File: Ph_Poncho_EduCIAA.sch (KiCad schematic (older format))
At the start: 26 parts, among them P1 BNC, U1 TC1121COA, U2 CA3140, U3 TL081

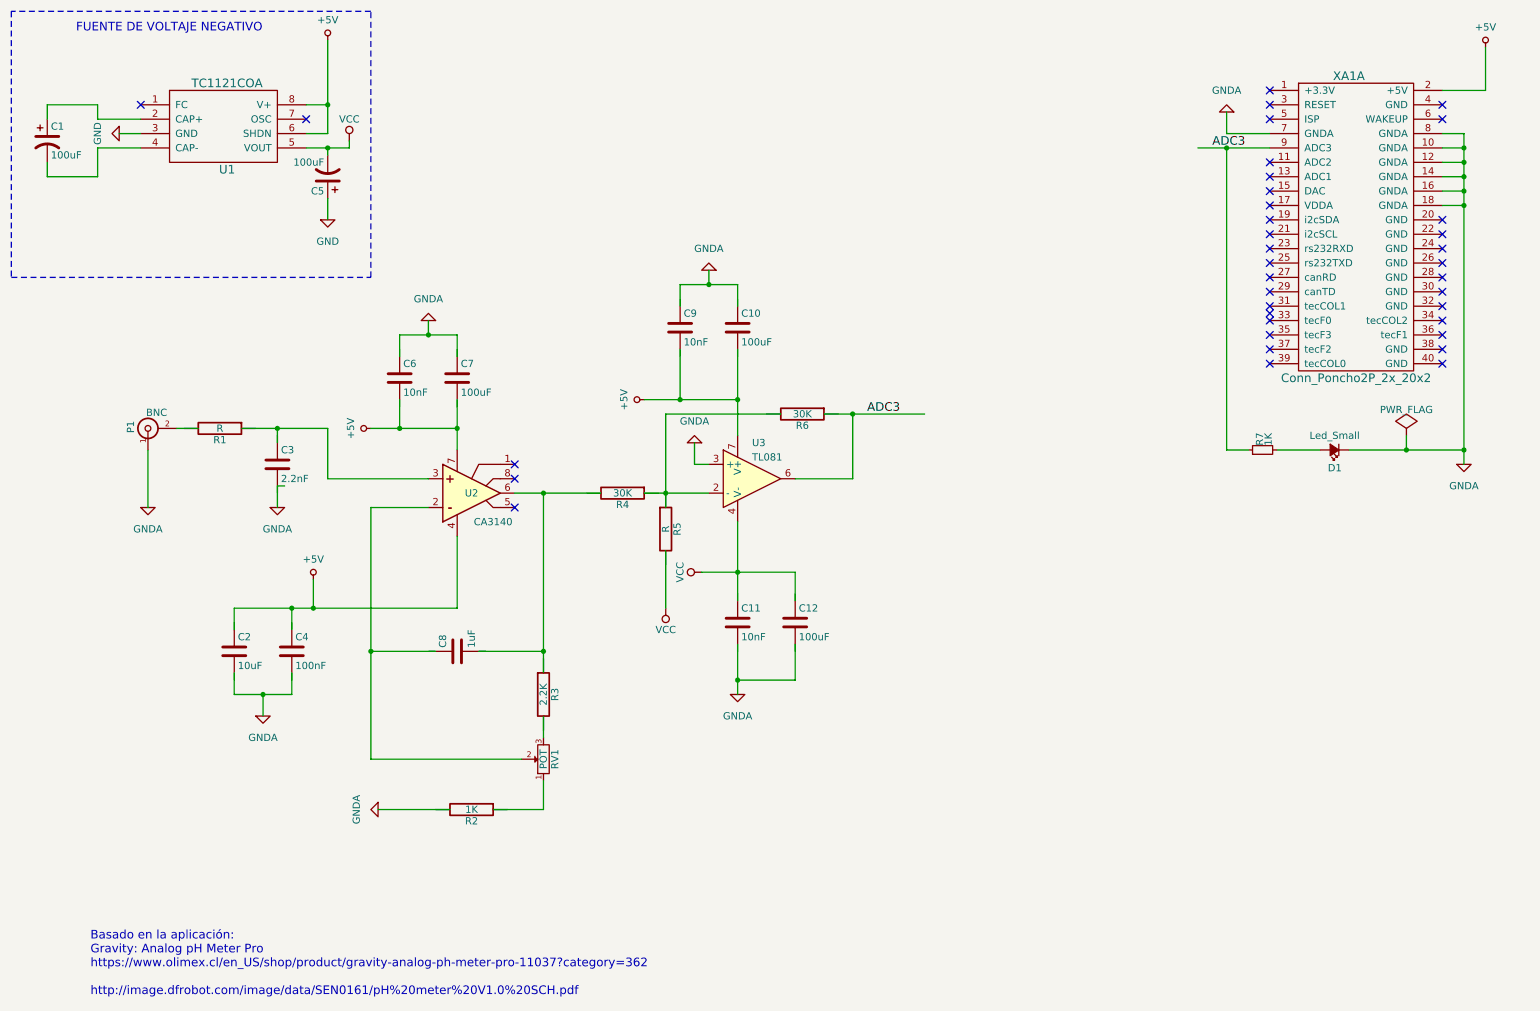
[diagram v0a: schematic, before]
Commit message: Se cambió el inversor de voltaje TC1121COA por el LMC7660
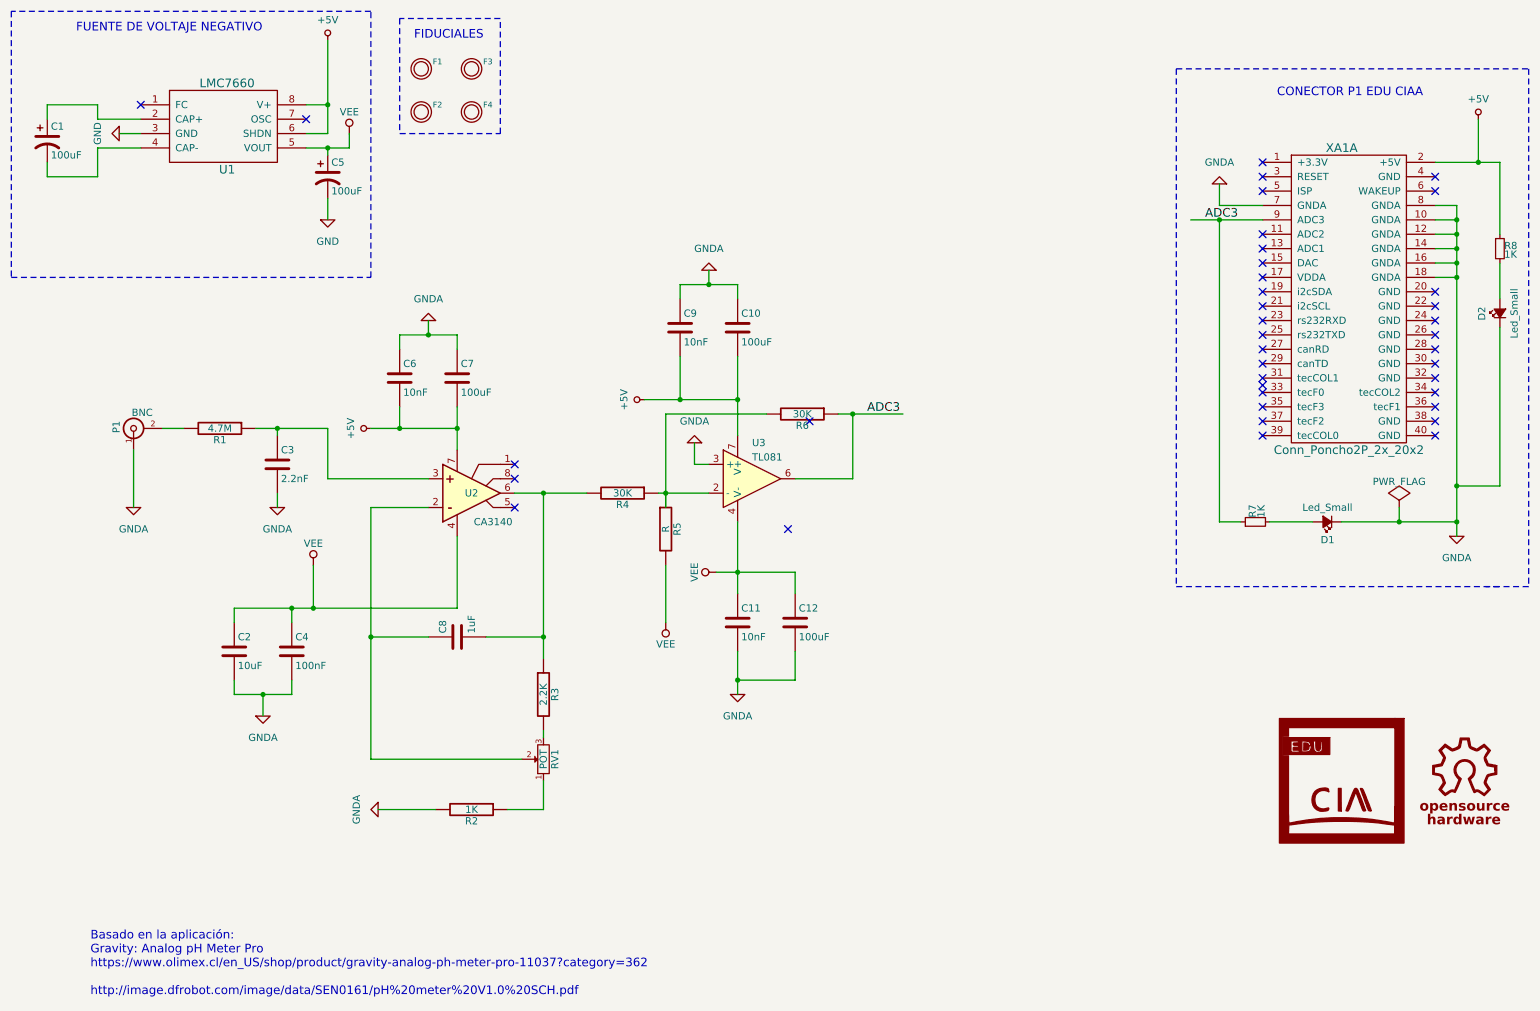
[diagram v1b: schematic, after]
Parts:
- removed U1: TC1121COA, symbol TC1121COA
- added D2: Led_Small, Ph_Poncho:LED_1206, symbol Led_Small
- added F1, F2, F3, F4: FIDUCIAL, Ph_Poncho:Fiducial_1mm, symbol FIDUCIAL
- added R8: 1K, Ph_Poncho:R_1206_HandSoldering, symbol R_Small
- added U1: LMC7660, symbol LMC7660
- C1: footprint (none) -> Ph_Poncho:CP_Elec_6.3x4.5; Digikey# Value -> 493-2203-1-ND; LibPart Value -> (none); Manf Value -> Nichicon; Manf# Value -> UWT1V101MCL1GS
- C10, C11, C12, C2, C3, C4, C6, C7, C8, C9: footprint (none) -> Ph_Poncho:C_1206_HandSoldering
- C5: footprint (none) -> Ph_Poncho:CP_Elec_6.3x4.5
- D1: footprint (none) -> Ph_Poncho:LED_1206; Digikey# (none) -> Value; LibPart (none) -> Value; Manf (none) -> Value; Manf# (none) -> Value; Mouser# (none) -> Value
- P1: footprint (none) -> Ph_Poncho:BNC_Socket_TYCO-AMP; Digikey# (none) -> A32244-ND; LibPart (none) -> Value; Manf (none) -> TE Connectivity AMP Connectors; Manf# (none) -> 5227161-1; Mouser# (none) -> Value
- R1: value R -> 4.7M; footprint (none) -> Ph_Poncho:R_1206_HandSoldering; Digikey# (none) -> Value; LibPart (none) -> Value; Manf (none) -> Value; Manf# (none) -> Value; Mouser# (none) -> Value
- R2, R3, R4, R5, R6, R7: footprint (none) -> Ph_Poncho:R_1206_HandSoldering
- RV1: footprint Potentiometers:Potentiometer_Trimmer_Bourns_3296Y -> Ph_Poncho:Potentiometer_Trimmer_Bourns_3296Y
- U2: footprint (none) -> Ph_Poncho:DIP-8_W7.62mm_Socket_LongPads; Digikey# (none) -> CA3140AEZ-ND; LibPart (none) -> Value; Manf (none) -> Intersil; Manf# (none) -> CA3140AEZ; Mouser# (none) -> Value
- U3: footprint (none) -> Ph_Poncho:DIP-8_W7.62mm_Socket_LongPads; Digikey# (none) -> 296-7203-5-ND; LibPart (none) -> Value; Manf (none) -> Texas Instruments; Manf# (none) -> TL081CP; Mouser# (none) -> Value
- XA1: footprint (none) -> Ph_Poncho:Conn_Poncho_Derecha; Digikey# (none) -> Value; LibPart (none) -> Value; Manf (none) -> Value; Manf# (none) -> Value; Mouser# (none) -> Value
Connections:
- net labels added: VEE
- net labels removed: VCC
- wire segments 90 -> 93
- no-connect marks 37 -> 39
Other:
- note added: "CONECTOR P1 EDU CIAA"
- note added: "FIDUCIALES"
- moved on the sheet: C8, D1, P1, R7, XA1A

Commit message: Nueva versión de esquemático
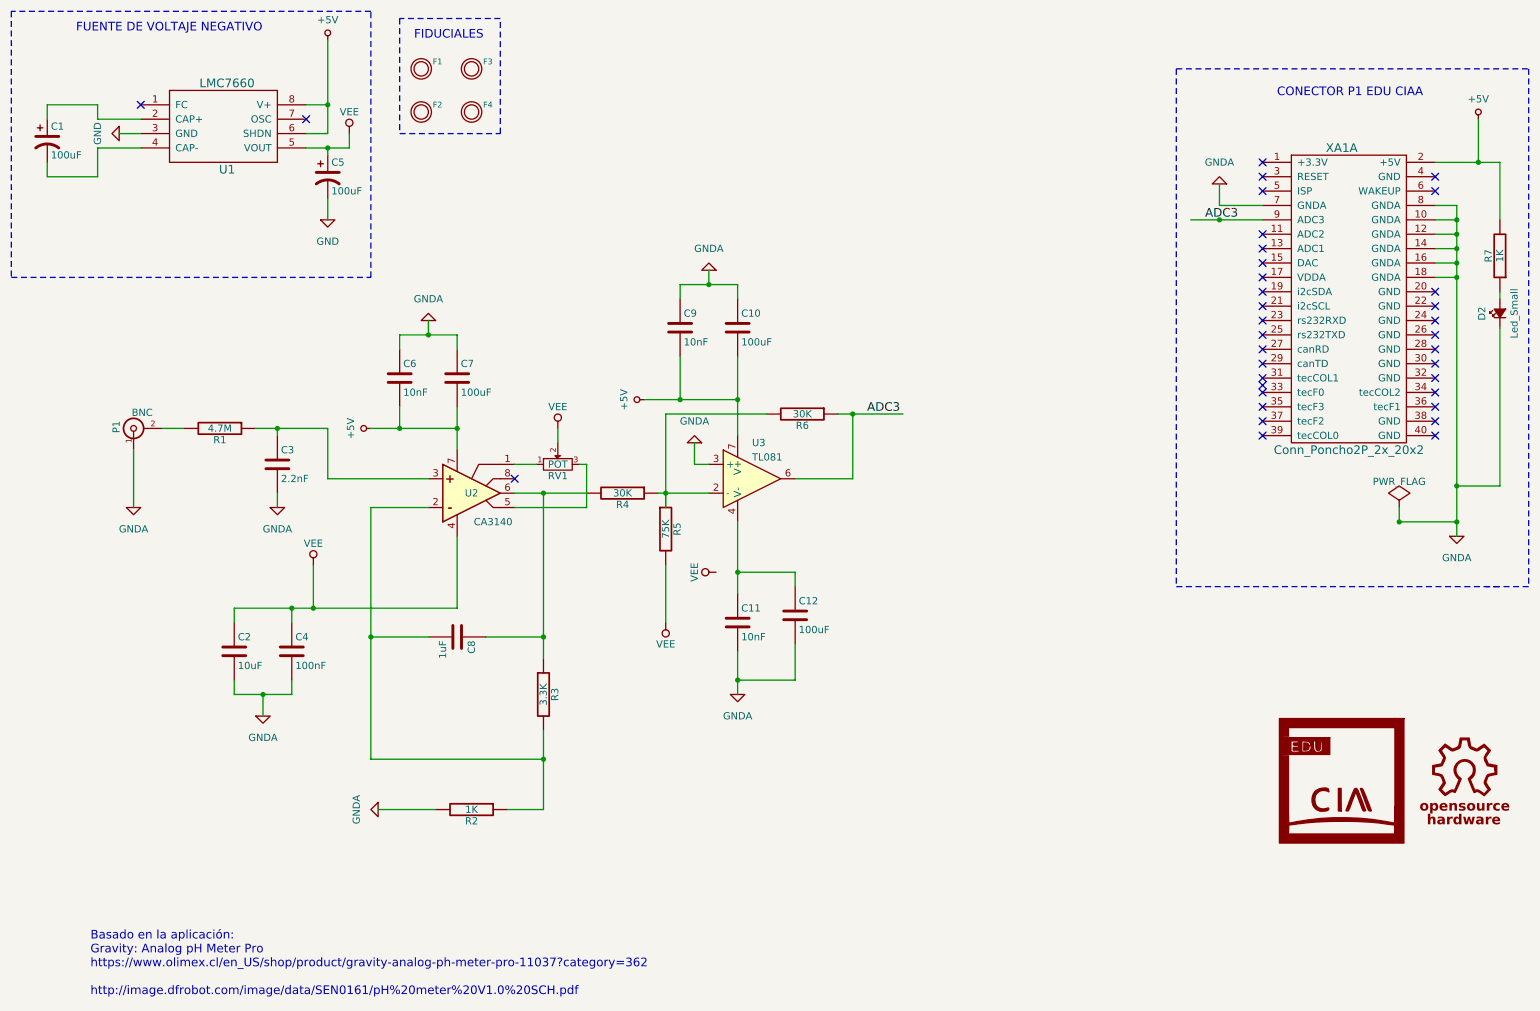
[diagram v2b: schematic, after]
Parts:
- removed D1: Led_Small, Ph_Poncho:LED_1206, symbol Led_Small
- removed R7, R8: 1K, Ph_Poncho:R_1206_HandSoldering, symbol R_Small
- added R7: 1K, Ph_Poncho:R_1206_HandSoldering, symbol R
- C1: LibPart (none) -> Value; Mouser# Value -> UWT1V101MCL1GS
- C10, C12, C7: Digikey# Value -> 490-13982-1-ND; Manf Value -> Murata Electronics North America; Manf# Value -> GRM31CR60J107KE39L; Mouser# Value -> 81-GRM31CR60J107KE9L
- C11, C6, C9: Digikey# Value -> 490-1754-2-ND; Manf Value -> Murata Electronics; Manf# Value -> GRM3195C1H103JA01D; Mouser# Value -> 81-GRM3195C1H103JA01
- C2, C8: Digikey# Value -> 399-9309-2-ND; Manf Value -> KEMET; Manf# Value -> C1206C106J4RACTU; Mouser# Value -> 80-C1206C106J4R
- C3: Digikey# Value -> 12063A222JAT2A-ND; Manf Value -> AVX Corporation; Manf# Value -> 12063A222JAT2A; Mouser# Value -> 581-12063A222JAT2
- C4: Digikey# Value -> 478-1129-1-ND; Manf Value -> AVX Corporation; Manf# Value -> http://datasheets.avx.com/cx5r.pdf
- C5: Digikey# Value -> 493-2203-1-ND; Manf Value -> Nichicon; Manf# Value -> UWT1V101MCL1GS; Mouser# Value -> UWT1V101MCL1GS
- D2: Digikey# Value -> 475-1410-2-ND; Manf Value -> OSRAM; Manf# Value -> LG R971-KN-1
- P1: Mouser# Value -> 571-5227161-1
- R1: Digikey# Value -> 311-4.7MERCT-ND; Manf Value -> Yageo; Manf# Value -> RC1206JR-074M7L; Mouser# Value -> 603-RC1206JR-074M7L
- R2: Digikey# Value -> 311-1.0KJRCT-ND; Manf Value -> Yageo; Manf# Value -> RC0402JR-071KL
- R3: value 2.2K -> 3.3K; Digikey# Value -> 311-3.3KERTR-ND; Manf Value -> Yageo; Manf# Value -> RC1206JR-073K3L; Mouser# Value -> 603-RC1206JR-073K3L
- R4, R6: Digikey# Value -> 311-30KERCT-ND; Manf Value -> Yageo; Manf# Value -> RC1206JR-0730KL; Mouser# Value -> 603-RC1206JR-0730KL
- R5: value R -> 75K; Digikey# (none) -> 311-75KERCT-ND; LibPart (none) -> Value; Manf (none) -> Yageo; Manf# (none) -> RC1206JR-0775KL; Mouser# (none) -> 03-RC1206JR-0775KL
- RV1: Digikey# PTD902-2015K-A503-ND -> 39255K-ND; Manf Value -> Honeywell Sensing and Productivity Solutions; Manf# Value -> 39255K
- U1: footprint (none) -> Ph_Poncho:SOIC-8-N; Digikey# (none) -> LMC7660IMX/NOPBCT-ND; LibPart (none) -> Value; Manf (none) -> LMC7660IMX/NOPB; Manf# (none) -> Value; Mouser# (none) -> LMC7660IMX/NOPB
- U2: Mouser# Value -> 968-CA3140AEZ
- U3: Mouser# Value -> 595-TL081CP
- XA1: Digikey# Value -> 952-1387-ND; Manf Value -> Harwin Inc.; Manf# Value -> M50-3502042; Mouser# Value -> 855-M50-3502042
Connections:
- net +5V: now also R7.2
- net VEE: now also RV1.2; no longer C11.1, C12.1, U3.4 (V-)
- net at U2.1 (BAL/COMP): now also RV1.1
- net at U2.5 (BALANCE): now also RV1.3
- net at R3.1, R4.2, U2.6 (OUTPUT): now also C8.1; no longer C8.2
- net at R3.2: now also C8.2, R2.1, U2.2 (INVERTING); no longer RV1.3
- net at D2.2 (A): now also R7.1
- new net: C11.1, C12.1, U3.4 (V-)
- no-connect marks 39 -> 35
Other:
- moved on the sheet: RV1

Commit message: Subiendo modificaciones, correcciones y primera versión de la placa ruteada y con planos de tierra
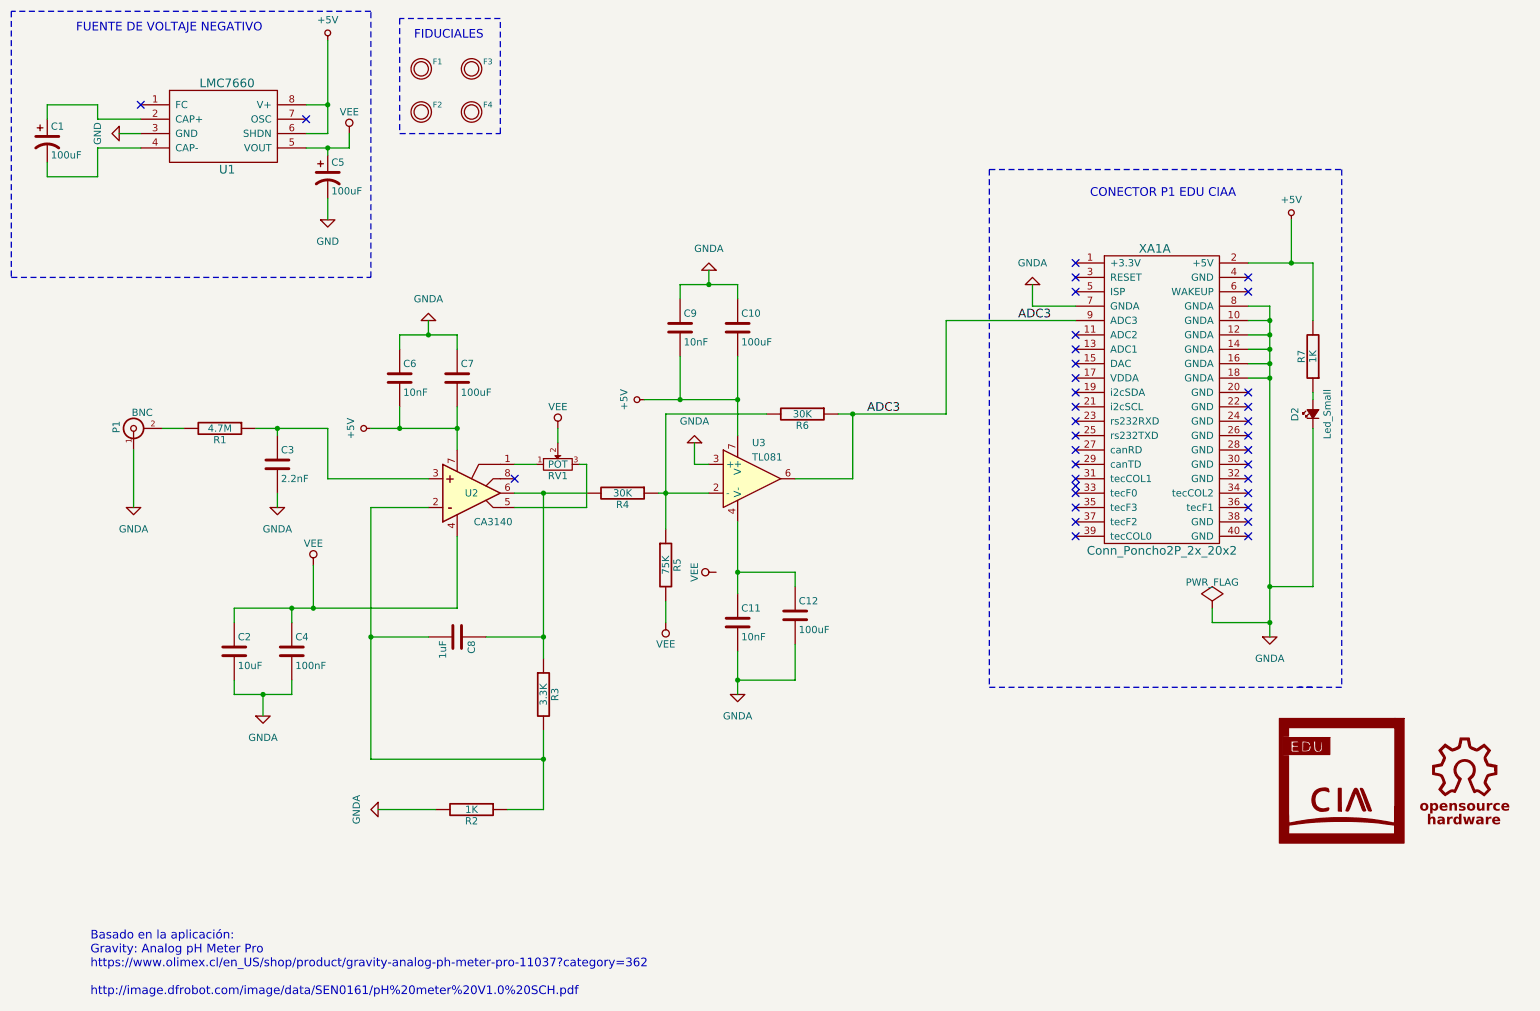
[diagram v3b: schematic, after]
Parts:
- U2, U3: footprint Ph_Poncho:DIP-8_W7.62mm_Socket_LongPads -> Ph_Poncho:SOIC-8-N
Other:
- moved on the sheet: D2, R5, R7, XA1A
